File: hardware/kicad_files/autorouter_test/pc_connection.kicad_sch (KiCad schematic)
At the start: 21 parts, among them U4 GT-USB-7010ASV, U5 FT232H

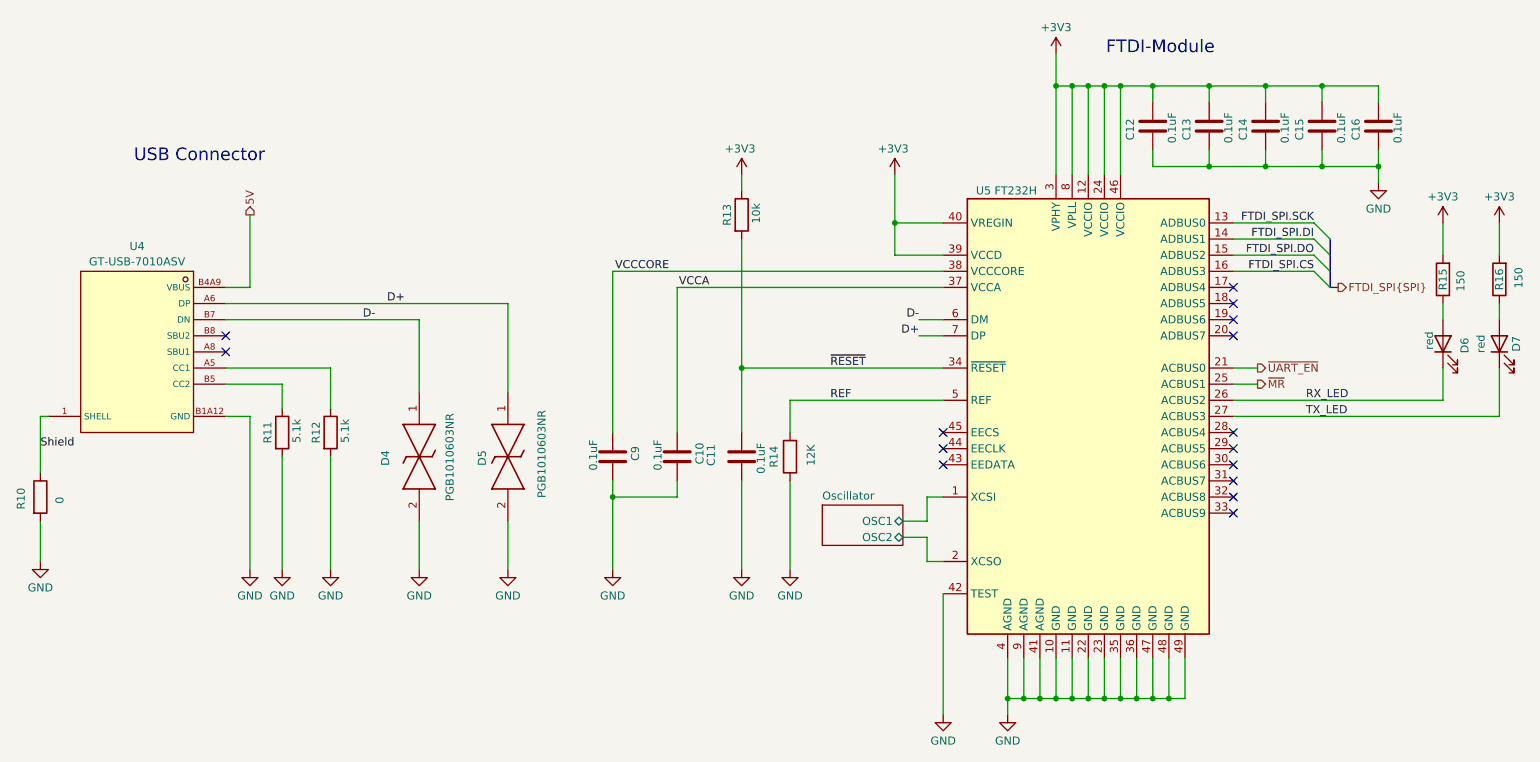
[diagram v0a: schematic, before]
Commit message: feat: first version of a complete layout. USB-C port might be problematic, FTDI chip does not have the best arrangement
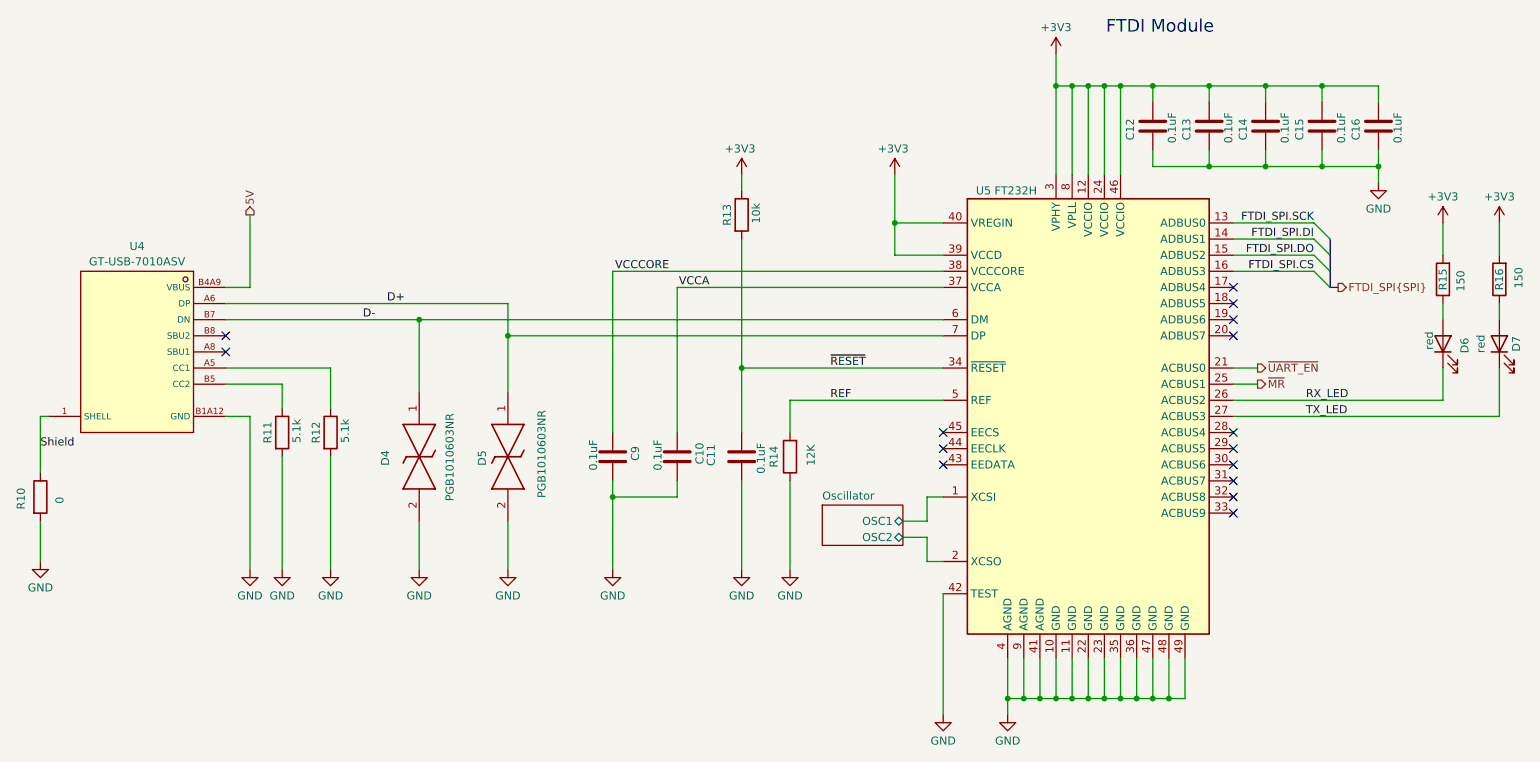
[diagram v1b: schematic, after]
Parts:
- U5: footprint Package_QFP:LQFP-48-1EP_7x7mm_P0.5mm_EP3.6x3.6mm -> Package_DFN_QFN:QFN-48-1EP_8x8mm_P0.5mm_EP6.2x6.2mm
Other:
- note added: "FTDI Module"
- note removed: "FTDI-Module"
- note removed: "USB Connector"
- title: PC connection -> (none)
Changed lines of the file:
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@@
 	(paper "A4")
 	(title_block
-		(title "PC connection")
 		(date "2024-05-30")
 		(rev "0.1")
@@
 	)
 	(junction
+		(at 91.44 88.9)
+		(diameter 0)
+		(color 0 0 0 0)
+	)
+	(junction
 		(at 201.93 52.07)
 		(diameter 0)
@@
 	)
 	(junction
+		(at 105.41 91.44)
+		(diameter 0)
+		(color 0 0 0 0)
+	)
+	(junction
 		(at 201.93 148.59)
 		(diameter 0)
@@
 	(wire
 		(pts
+			(xy 105.41 91.44) (xy 173.99 91.44)
+		)
+		(stroke
+			(width 0)
+			(type default)
+		)
+	)
+	(wire
+		(pts
 			(xy 69.85 110.49) (xy 69.85 128.27)
 		)
@@
 	(wire
 		(pts
-			(xy 167.64 123.19) (xy 171.45 123.19)
+			(xy 91.44 88.9) (xy 173.99 88.9)
 		)
 		(stroke
@@
 	(wire
 		(pts
-			(xy 149.86 101.6) (xy 173.99 101.6)
+			(xy 167.64 123.19) (xy 171.45 123.19)
 		)
 		(stroke
@@
 	(wire
 		(pts
-			(xy 252.73 101.6) (xy 252.73 96.52)
+			(xy 149.86 101.6) (xy 173.99 101.6)
 		)
 		(stroke
@@
 		)
 	)
-	(bus
+	(wire
 		(pts
-			(xy 234.95 83.82) (xy 236.22 83.82)
+			(xy 252.73 101.6) (xy 252.73 96.52)
 		)
 		(stroke
@@
 		)
 	)
-	(wire
+	(bus
 		(pts
-			(xy 252.73 86.36) (xy 252.73 88.9)
+			(xy 234.95 83.82) (xy 236.22 83.82)
 		)
 		(stroke
@@
 	(wire
 		(pts
-			(xy 215.9 64.77) (xy 207.01 64.77)
+			(xy 252.73 86.36) (xy 252.73 88.9)
 		)
 		(stroke
@@
 	(wire
 		(pts
-			(xy 170.18 91.44) (xy 173.99 91.44)
+			(xy 215.9 64.77) (xy 207.01 64.77)
 		)
 		(stroke
@@
 	(wire
 		(pts
-			(xy 105.41 86.36) (xy 105.41 100.33)
+			(xy 105.41 86.36) (xy 105.41 91.44)
 		)
 		(stroke
@@
 	(wire
 		(pts
-			(xy 170.18 88.9) (xy 173.99 88.9)
-		)
-		(stroke
-			(width 0)
-			(type default)
-		)
-	)
-	(wire
-		(pts
 			(xy 194.31 148.59) (xy 196.85 148.59)
 		)
@@
 	(wire
 		(pts
+			(xy 105.41 91.44) (xy 105.41 100.33)
+		)
+		(stroke
+			(width 0)
+			(type default)
+		)
+	)
+	(wire
+		(pts
 			(xy 232.41 73.66) (xy 219.71 73.66)
 		)
@@
 		)
 	)
-	(text "USB Connector"
-		(exclude_from_sim no)
-		(at 46.482 64.262 0)
-		(effects
-			(font
-				(size 2 2)
-			)
-			(justify left bottom)
-		)
-	)
-	(text "FTDI-Module\n"
+	(text "FTDI Module\n\n"
 		(exclude_from_sim no)
 		(at 199.644 47.244 0)
@@
 		)
 	)
-	(label "D+"
-		(at 170.18 91.44 180)
-		(fields_autoplaced yes)
-		(effects
-			(font
-				(size 1.27 1.27)
-			)
-			(justify right bottom)
-		)
-	)
 	(label "RX_LED"
 		(at 231.14 101.6 0)
@@
 		)
 	)
-	(label "D-"
-		(at 170.18 88.9 180)
-		(fields_autoplaced yes)
-		(effects
-			(font
-				(size 1.27 1.27)
-			)
-			(justify right bottom)
-		)
-	)
 	(label "D+"
 		(at 86.36 86.36 0)
@@
 			)
 		)
-		(property "Footprint" "Package_QFP:LQFP-48-1EP_7x7mm_P0.5mm_EP3.6x3.6mm"
+		(property "Footprint" "Package_DFN_QFN:QFN-48-1EP_8x8mm_P0.5mm_EP6.2x6.2mm"
 			(at 196.85 104.14 0)
 			(effects
